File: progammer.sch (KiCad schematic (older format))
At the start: 4 parts

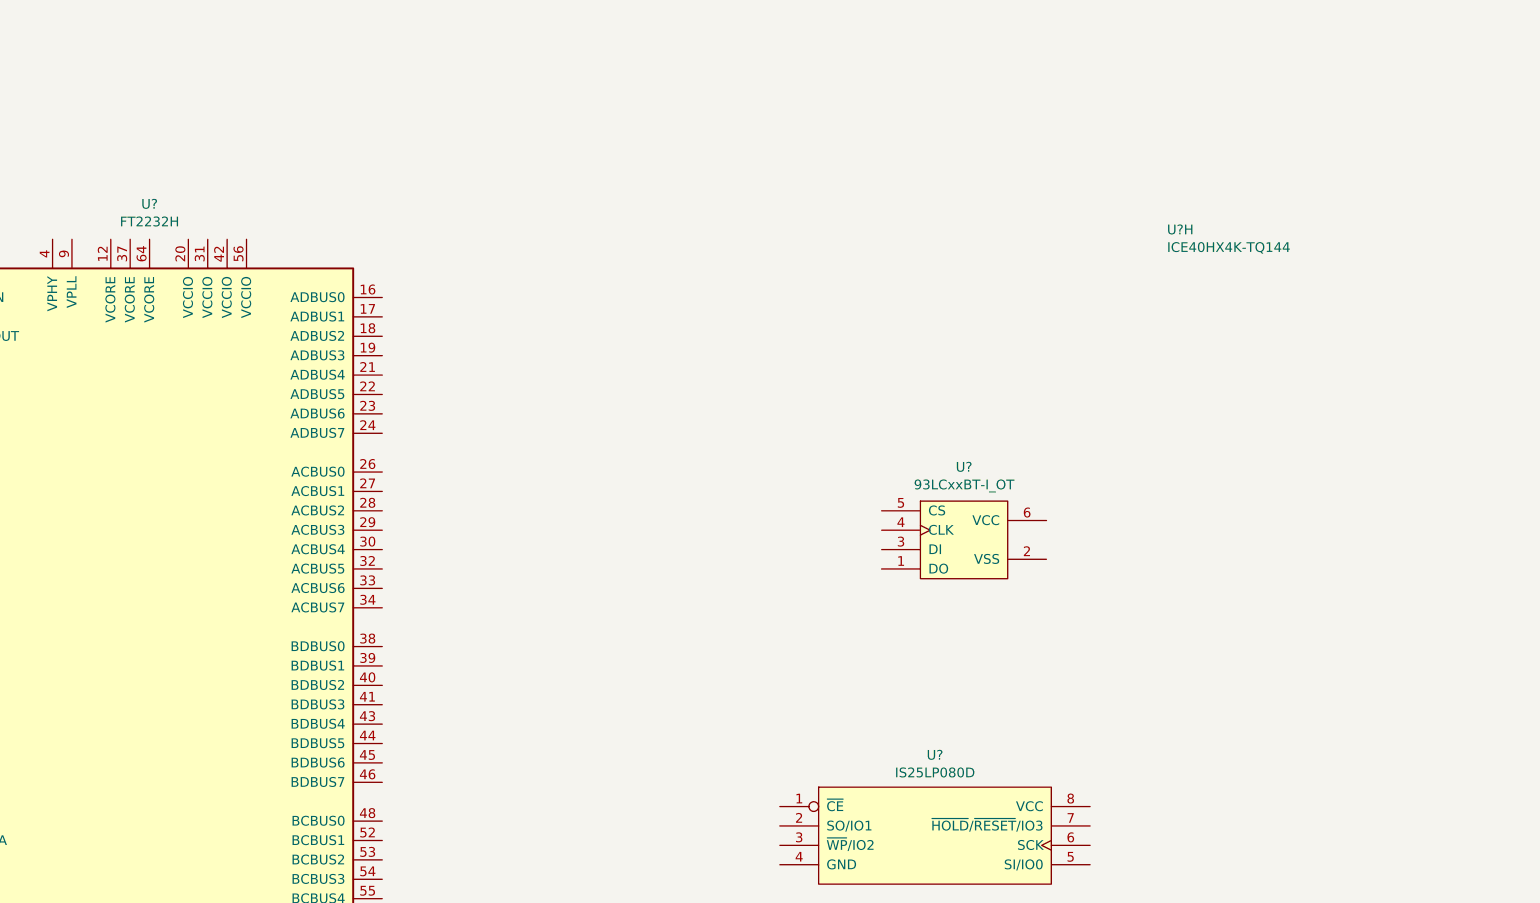
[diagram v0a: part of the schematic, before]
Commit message: Made a overview on the toplevel schematic and added the SRAM subschematic.
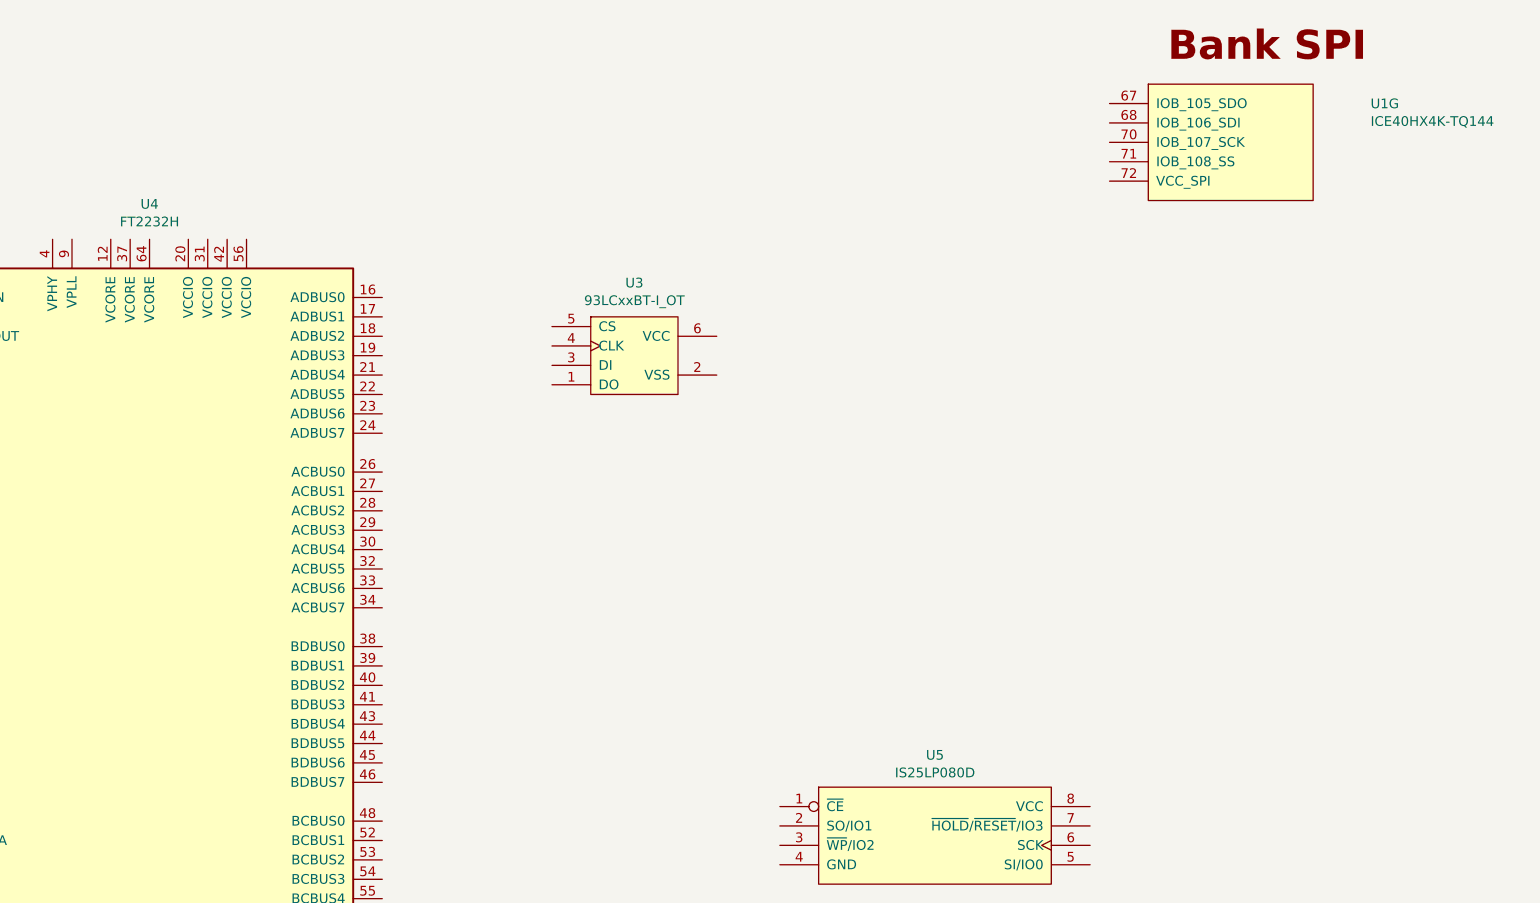
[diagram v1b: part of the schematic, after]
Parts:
- removed U?: ICE40HX4K-TQ144, symbol ice40hx4k:ICE40HX4K-TQ144
- added U1: ICE40HX4K-TQ144, symbol ice40hx4k:ICE40HX4K-TQ144
- gave numbers to parts that had none: 3
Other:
- moved on the sheet: U3
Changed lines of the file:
@@
 EESchema Schematic File Version 4
+LIBS:ice40_breakout-cache
 EELAYER 29 0
 EELAYER END
 $Descr A4 11693 8268
 encoding utf-8
-Sheet 4 5
+Sheet 5 6
 Title ""
 Date ""
@@
 $EndDescr
 $Comp
-L Interface_USB:FT2232H U?
+L Interface_USB:FT2232H U4
 U 1 1 5CAB920B
 P 4125 4375
-F 0 "U?" H 4125 6756 50  0000 C CNN
+F 0 "U4" H 4125 6756 50  0000 C CNN
 F 1 "FT2232H" H 4125 6665 50  0000 C CNN
 F 2 "" H 4125 4375 50  0001 C CNN
@@
 $EndComp
 $Comp
-L 93LCxxBT:93LCxxBT-I_OT U?
+L 93LCxxBT:93LCxxBT-I_OT U3
 U 1 1 5CABEF2A
-P 8350 3725
-F 0 "U?" H 8325 4100 50  0000 C CNN
-F 1 "93LCxxBT-I_OT" H 8325 4009 50  0000 C CNN
-F 2 "Package_TO_SOT_SMD:SOT-23-6" H 8350 4025 50  0001 C CNN
-F 3 "http://ww1.microchip.com/downloads/en/DeviceDoc/21794G.pdf" H 8300 3475 50  0001 C CNN
-	1    8350 3725
+P 6650 2775
+F 0 "U3" H 6625 3150 50  0000 C CNN
+F 1 "93LCxxBT-I_OT" H 6625 3059 50  0000 C CNN
+F 2 "Package_TO_SOT_SMD:SOT-23-6" H 6650 3075 50  0001 C CNN
+F 3 "http://ww1.microchip.com/downloads/en/DeviceDoc/21794G.pdf" H 6600 2525 50  0001 C CNN
+	1    6650 2775
 	1    0    0    -1
 $EndComp
 $Comp
-L IS25LP080D:IS25LP080D U?
+L IS25LP080D:IS25LP080D U5
 U 1 1 5CAC0F76
 P 8175 5250
-F 0 "U?" H 8175 5665 50  0000 C CNN
+F 0 "U5" H 8175 5665 50  0000 C CNN
 F 1 "IS25LP080D" H 8175 5574 50  0000 C CNN
 F 2 "Package_SO:SO-8_3.9x4.9mm_P1.27mm" H 8175 4850 50  0001 C CNN
@@
 $EndComp
 $Comp
-L ice40hx4k:ICE40HX4K-TQ144 U?
-U 8 1 5CADBC7F
-P 8225 2325
-F 0 "U?" H 9371 2524 50  0000 L CNN
-F 1 "ICE40HX4K-TQ144" H 9371 2433 50  0000 L CNN
-F 2 "" H 8225 2325 50  0001 C CNN
-F 3 "" H 8225 2325 50  0001 C CNN
-	8    8225 2325
+L ice40hx4k:ICE40HX4K-TQ144 U1
+U 7 1 5CABE304
+P 9275 1675
+F 0 "U1" H 10421 1874 50  0000 L CNN
+F 1 "ICE40HX4K-TQ144" H 10421 1783 50  0000 L CNN
+F 2 "" H 9275 1675 50  0001 C CNN
+F 3 "" H 9275 1675 50  0001 C CNN
+	7    9275 1675
 	1    0    0    -1
 $EndComp

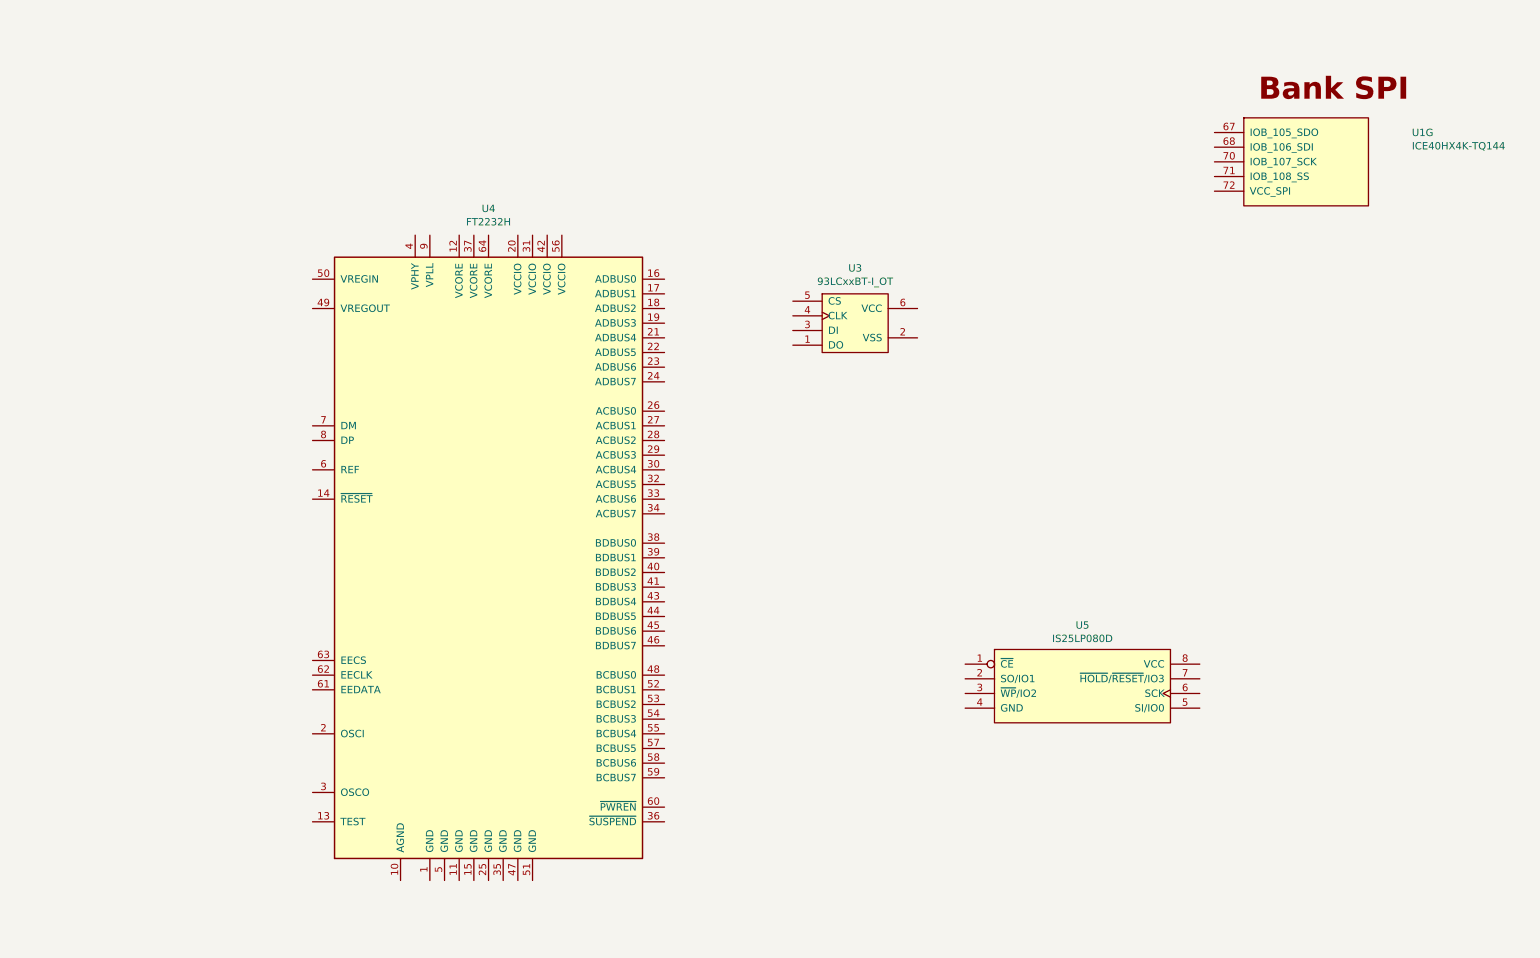
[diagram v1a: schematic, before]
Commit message: sram, ui, power, flash and header
SRAM: mostly done. Changed the choosen IC to a faster one in a differenc housing.

POWER: added some step down converter for 3.3 V and 1.2 V. The 1.2 V is oversized and could be changed to a smaller one

Programmer: added flash.

HEADER: Added Arduino Uno like headers with 5 V signal level. Analog is not connected now, will get an I2C ADC in future. Also added 3 digilent pmod styled connector with 3.3 V signal level.

UI: added 5 buttons and 8 LEDs. There is some space left over, maybe double the LED count in future.
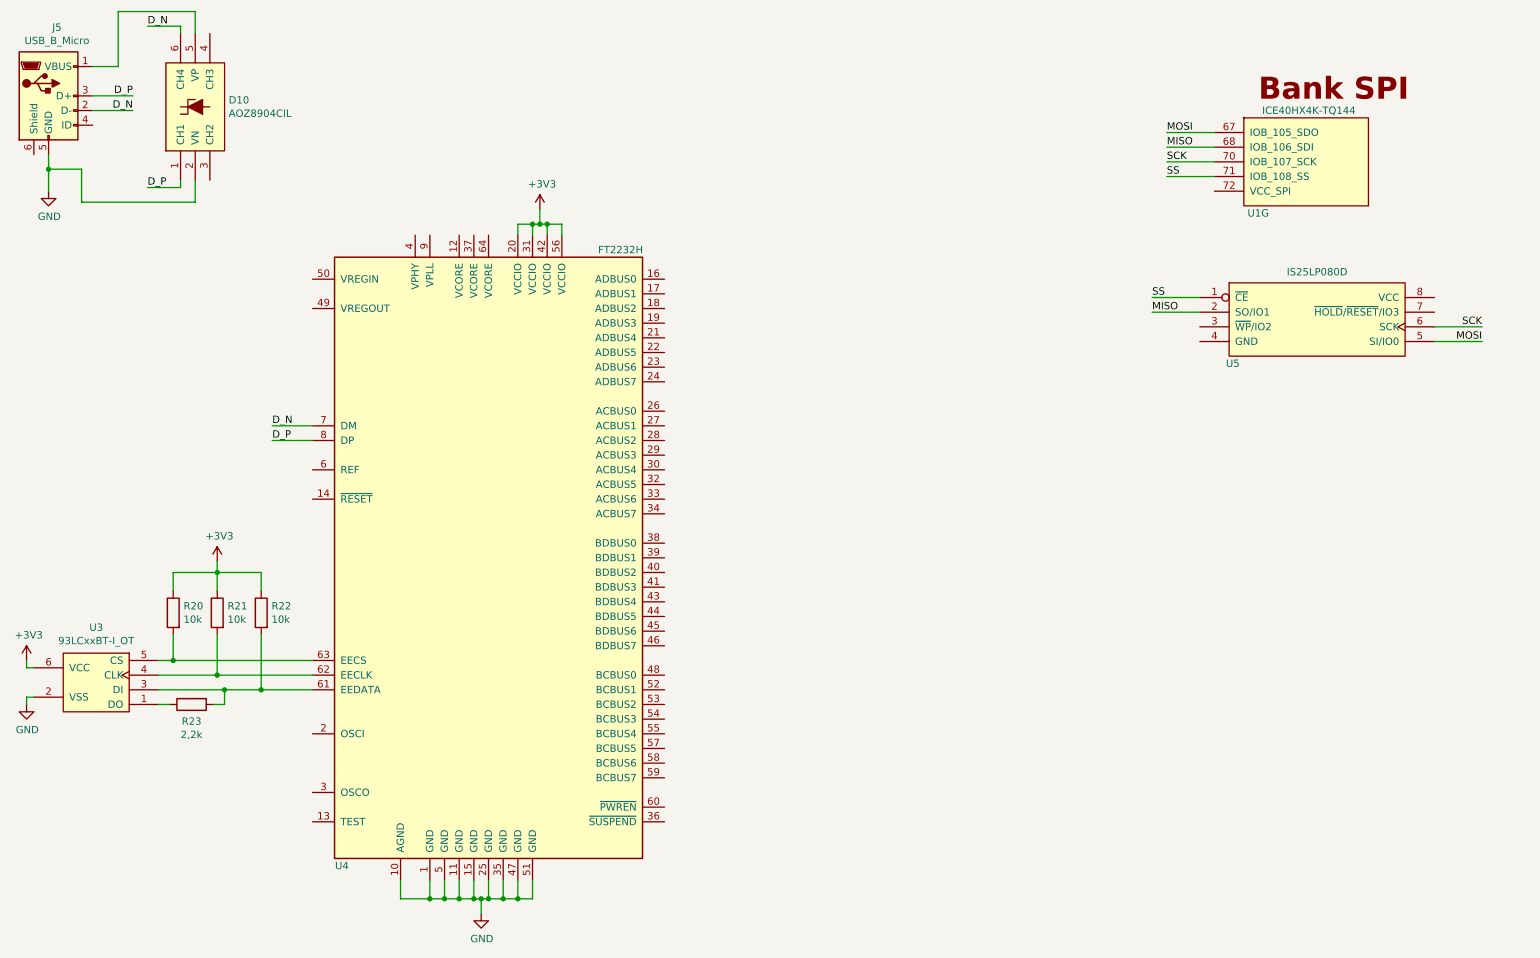
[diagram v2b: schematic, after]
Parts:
- added D10: AOZ8904CIL, Package_TO_SOT_SMD:SOT-23-6, symbol AOZ8904CIL:AOZ8904CIL
- added J5: USB_B_Micro, footprints:Amphenol_microUSB_B_footprint, symbol Connector:USB_B_Micro
- added R20, R21, R22: 10k, Resistor_SMD:R_0603_1608Metric, symbol Device:R
- added R23: 2,2k, Resistor_SMD:R_0603_1608Metric, symbol Device:R
- U4: footprint (none) -> Package_QFP:LQFP-64_10x10mm_P0.5mm
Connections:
- net GND: now reaches U4.1 (GND)
- net GND: now also U3.2 (VSS), U4.10 (AGND), U4.11 (GND), U4.15 (GND), U4.25 (GND), U4.35 (GND), U4.47 (GND), U4.5 (GND), U4.51 (GND), D10.2 (VN), J5.5 (GND)
- net +3V3: now reaches U4.20 (VCCIO)
- net +3V3: now also U3.6 (VCC), U4.31 (VCCIO), U4.42 (VCCIO), U4.56 (VCCIO), R20.1, R21.1, R22.1
- net at U4.61 (EEDATA): now also U3.3 (DI), R22.2, R23.2
- net at U4.62 (EECLK): now also U3.4 (CLK), R21.2
- net at U4.63 (EECS): now also U3.5 (CS), R20.2
- net D_N: now reaches U4.7 (DM)
- net D_N: now also D10.6 (CH4), J5.2 (D-)
- net D_P: now reaches U4.8 (DP)
- net D_P: now also D10.1 (CH1), J5.3 (D+)
- net MOSI: now reaches U1.67 (IOB_105_SDO)
- net MOSI: now also U5.5 (SI/IO0)
- net MISO: now reaches U1.68 (IOB_106_SDI)
- net MISO: now also U5.2 (SO/IO1)
- net SCK: now reaches U1.70 (IOB_107_SCK)
- net SCK: now also U5.6 (SCK)
- net SS: now reaches U1.71 (IOB_108_SS)
- net SS: now also U5.1 (~CE~)
- net at U3.1 (DO): now also R23.1
- new net: D10.5 (VP), J5.1 (VBUS)
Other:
- moved on the sheet: U3, U5
